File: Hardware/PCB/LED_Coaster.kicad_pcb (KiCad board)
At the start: 2 copper layers, 90 x 90 mm, 88 parts, among them J1 Li-po, J3 USB_C_Receptacle_USB2.0_16P, J4 UART, Q1 AO3401A, SW1 SW_SPDT, U1 ESP32-C3-WROOM-02-H4, U3 MCP73871-2CC, U4 TLV75533PDBVR

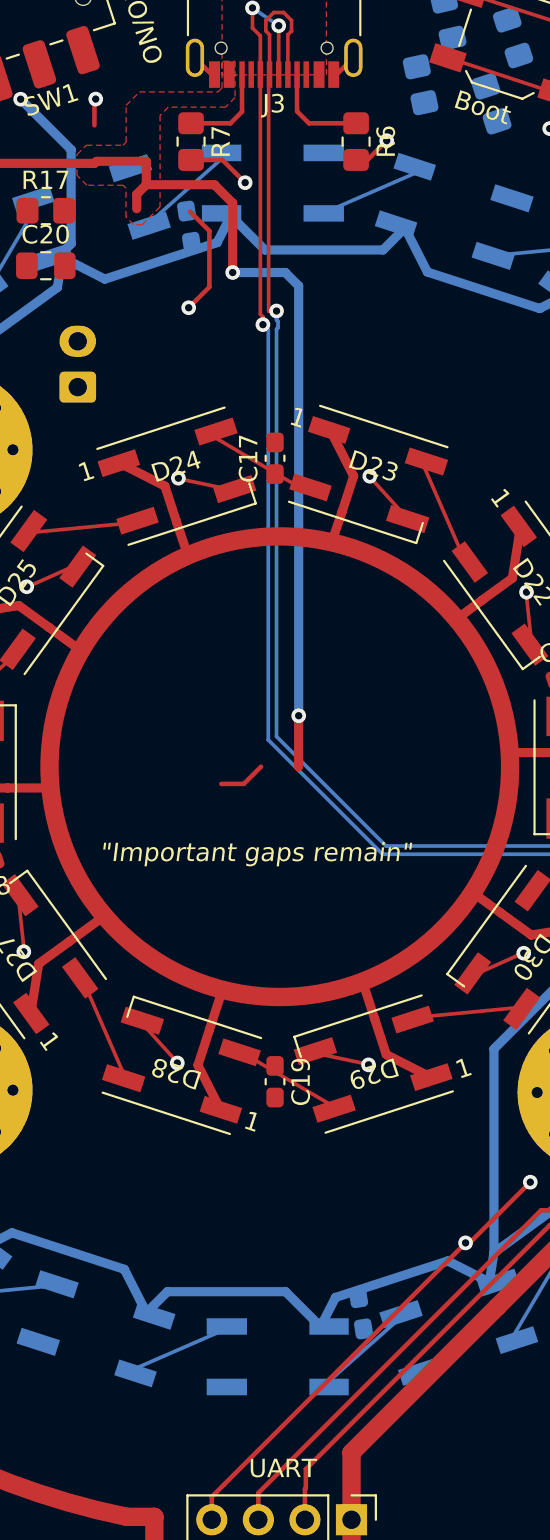
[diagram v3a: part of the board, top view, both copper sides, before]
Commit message: Move C10/C14 outward, and restructure Phase 5 as a numbered action list
C10 and C14 sit in the two tightest gaps on the outer ring, so at the exact
midpoint bearing they overlapped D7 and D17 by 0.07 mm. They were nudged 1°
sideways, which left them visibly off-centre in the slot. Moving them outward
to r = 35 instead puts them back on the midpoint bearing with the round
rotations the other six use, and widens their clearance to +1.40/+0.81 mm - the
roomiest on the ring. Outward also keeps every capacitor at or beyond the LED
radius, so nothing encroaches on the battery pocket in the middle of the back.

Phase 5 was hard to act on: reference material and steps were interleaved. It
is now one background block followed by nine numbered actions.

Action 2 is new. Deleting the three dead zones also removed the only GND zone
on F.Cu - it was a 3 x 4 mm scrap sitting on the old regulator. The back keeps
its board-wide pour but the front now has none, which is why 47 ground pads
read as isolated: every front LED D21-D30, all four buttons, the four front
decoupling caps and the whole new power section. A board-wide F.Cu GND zone
connects them in one step.

Connectivity re-measured with all 34 parts placed, so the scope table is
current: +LED_PWR needs ~40 connections (46 pads in 41 groups), +SYS 8,
+BATT 5, /BAT_SENSE 3, +3V3 2, plus the 28 LED data hops.

Co-Authored-By: Claude Opus 5 <noreply@anthropic.com>
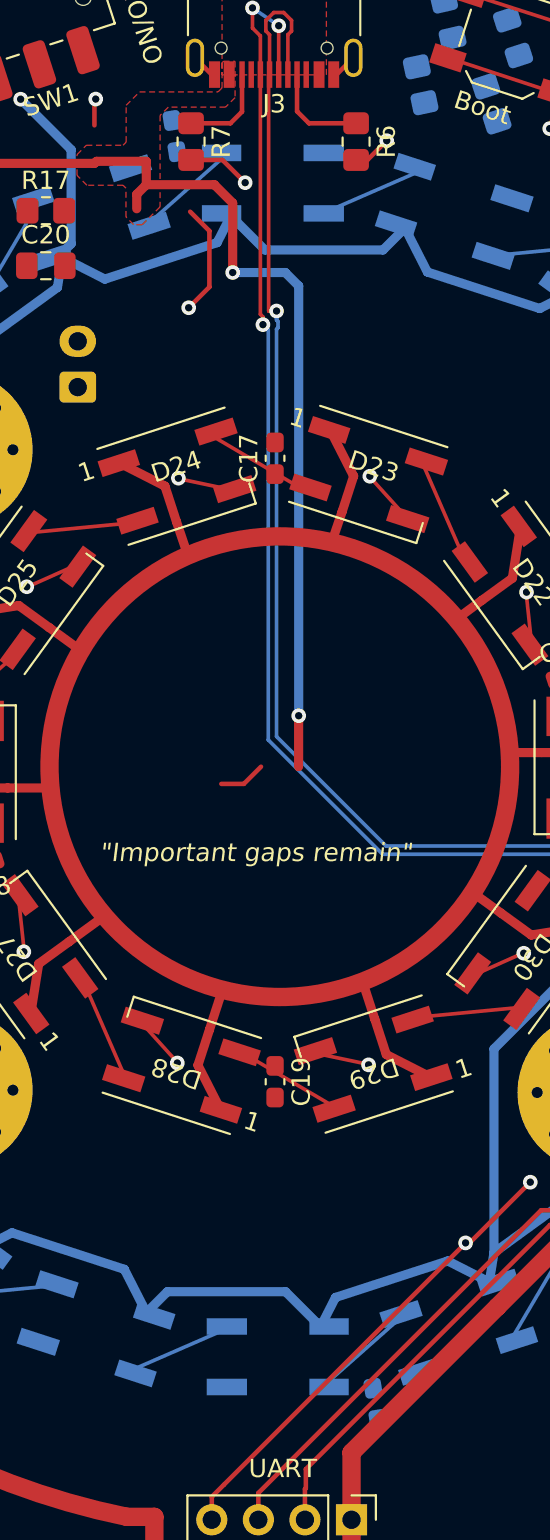
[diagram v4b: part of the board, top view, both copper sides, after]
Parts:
- moved C10 5.00 mm to (144.5, 45.4)
- moved C14 5.00 mm to (155.5, 114.6)
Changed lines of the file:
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@@
 	(footprint "Capacitor_SMD:C_0603_1608Metric_Pad1.08x0.95mm_HandSolder"
 		(layer "B.Cu")
-		(at 145.31 50.37 99)
+		(at 144.52 45.43 99)
 		(descr "Capacitor SMD 0603 (1608 Metric), square (rectangular) end terminal, IPC-7351 nominal with elongated pad for handsoldering. (Body size source: IPC-SM-782 page 76, https://www.pcb-3d.com/wordpress/wp-content/uploads/ipc-sm-782a_amendment_1_and_2.pdf)")
 		(tags "capacitor handsolder")
@@
 	(footprint "Capacitor_SMD:C_0603_1608Metric_Pad1.08x0.95mm_HandSolder"
 		(layer "B.Cu")
-		(at 154.69 109.63 -81)
+		(at 155.48 114.57 -81)
 		(descr "Capacitor SMD 0603 (1608 Metric), square (rectangular) end terminal, IPC-7351 nominal with elongated pad for handsoldering. (Body size source: IPC-SM-782 page 76, https://www.pcb-3d.com/wordpress/wp-content/uploads/ipc-sm-782a_amendment_1_and_2.pdf)")
 		(tags "capacitor handsolder")

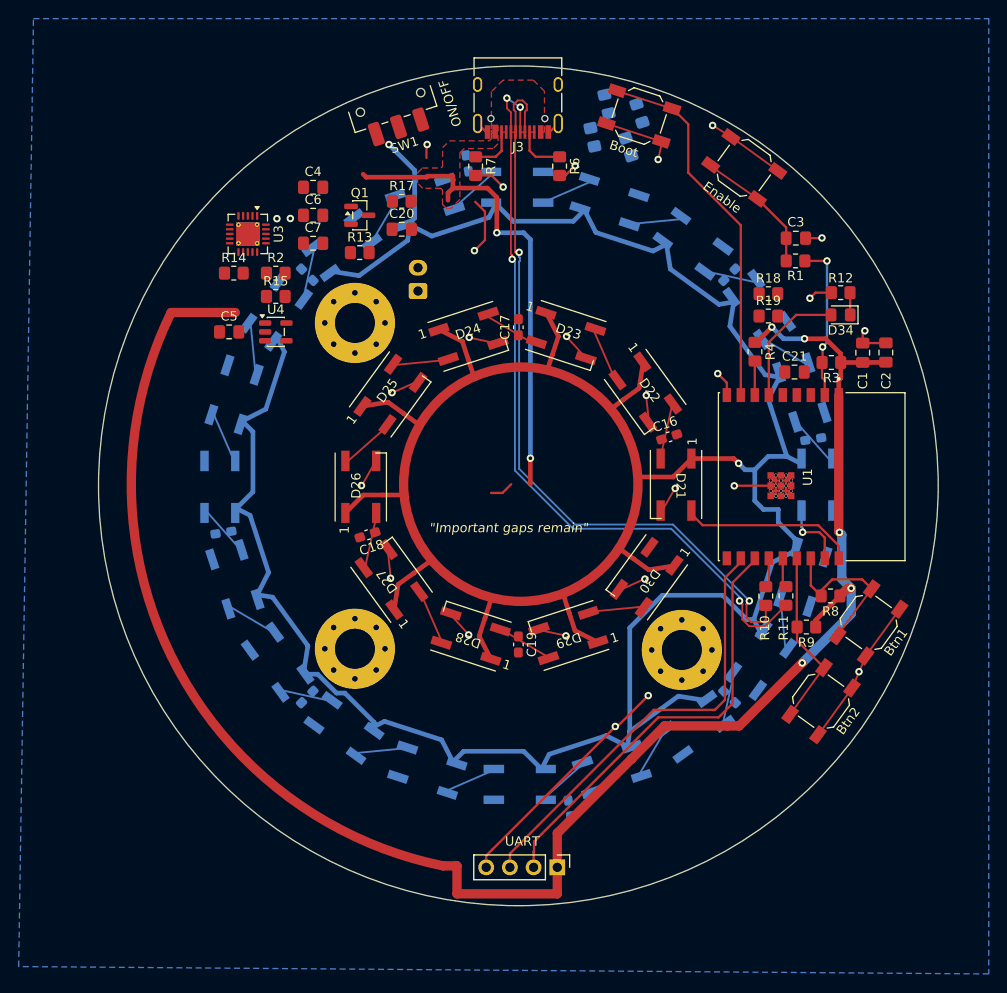
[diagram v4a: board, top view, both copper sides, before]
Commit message: Add pcb_check.py, a standalone board analysis tool, and document it
Every board question in this project so far has been answered by writing a
throwaway parser, and several of those parsers were wrong in ways that produced
confident bad advice. This commits one tool instead, and records the traps.

Hardware/PCB/tools/pcb_check.py reads LED_Coaster.kicad_pcb directly - stdlib
only, no KiCad install. Subcommands: nets, net <NAME>, shorts, rings, zones,
widths, placement, all. KiCad DRC stays the authority on manufacturability;
this answers what DRC does not, namely whether a net is genuinely one island
and which pad is stranded.

Six parsing traps are encoded in the header comment, each of which caused a
wrong answer at least once:

- Back-side pads are NOT X-mirrored. Mirroring swaps pad 3 for pad 4, invents
  shorts, and made a uniform LED ring look like it fanned through five
  orientations. Caught only when the PCB editor was read directly.
- A track end inside a via's pad radius is connected, not merely near it.
- Zone fills carry a per-polygon layer tag; one zone can span both sides.
- Same-net zones whose fills touch are one island, and priority decides
  overlaps, so a higher-priority zone can orphan a lower one.
- Pads sharing a number on one footprint are internally connected.
- Fine-pitch rectangular pads must not be approximated by their circumradius.

Also commits the routing done in Phase 5 actions 1-7.

Co-Authored-By: Claude Opus 5 <noreply@anthropic.com>
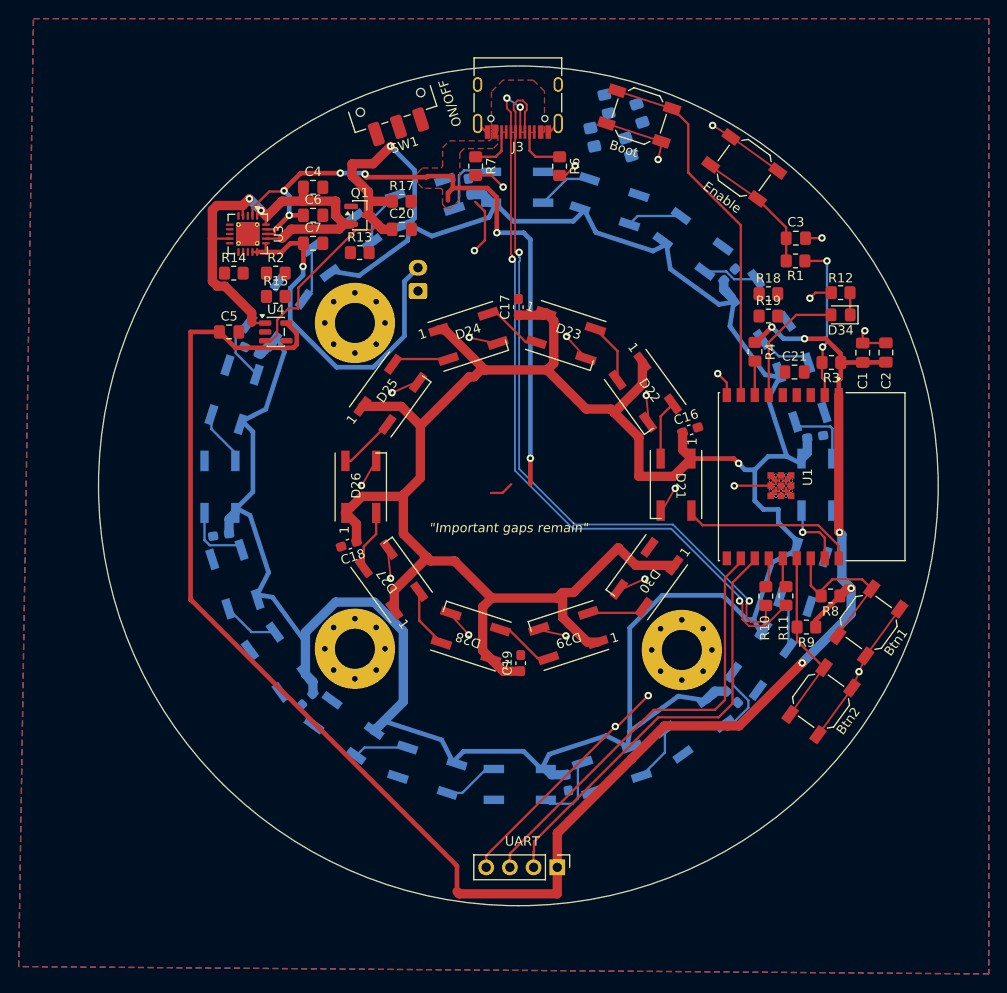
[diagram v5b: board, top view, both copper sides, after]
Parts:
- moved C11 10.1 mm to (121.4, 65.5), turned to 155 degrees
- moved C14 2.76 mm to (155.2, 111.8)
- moved C10 2.51 mm to (144.8, 47.9)
- moved C16 2.37 mm to (168.4, 74.0)
- moved C18 2.24 mm to (131.8, 86.2)
- moved C17 2.16 mm to (150.0, 60.8)
- moved C19 2.02 mm to (150.2, 99.0), turned to 90 degrees
- moved C12 0.35 mm to (118.1, 85.3)
- moved C8 0.33 mm to (181.8, 74.7)
- moved C15 0.25 mm to (172.9, 102.6)
- moved C13 0.25 mm to (127.4, 102.9)
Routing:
- net +LED_PWR: track 290.8 -> 473.6 mm
- net +3V3: track 95.3 -> 196.0 mm
- net +SYS: track 0.00 -> 49.7 mm, vias 0 -> 2
- net +BATT: track 0.00 -> 39.4 mm, vias 0 -> 1
- net +5V: track 51.6 -> 75.2 mm, vias 2 -> 6
- net Net-(D16-DOUT): track 0.00 -> 7.91 mm
- net Net-(D18-DOUT): track 0.00 -> 7.69 mm
- net Net-(D6-DOUT): track 0.00 -> 7.56 mm
- net Net-(D1-DOUT): track 0.00 -> 7.54 mm
- net Net-(D11-DOUT): track 0.00 -> 7.33 mm
- net Net-(D10-DIN): track 0.00 -> 7.03 mm
- net Net-(D22-DOUT): track 0.00 -> 6.46 mm
- net Net-(D27-DOUT): track 0.00 -> 6.45 mm
- net Net-(D28-DOUT): track 0.00 -> 6.43 mm
- net Net-(D26-DOUT): track 0.00 -> 6.42 mm
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- added copper zone on F.Cu, net GND

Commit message: Close the last outer-ring data hop, D13 to D14
Five B.Cu segments detouring around C13. That completes phase 5
action 5: the outer chain is 19 of 19 hops, and with the inner ring
already done both data chains are continuous end to end.

Co-Authored-By: Claude Opus 5 <noreply@anthropic.com>
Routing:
- net Net-(D13-DOUT): track 0.00 -> 7.57 mm
- net GND: track 72.2 -> 74.3 mm
- net +SYS: track 49.7 -> 50.4 mm
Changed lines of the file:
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@@
 	)
 	(segment
+		(start 121 50.106808)
+		(end 121.051808 50.055)
+		(width 0.25)
+		(layer "F.Cu")
+		(net "GND")
+	)
+	(segment
 		(start 182.52 53.45)
 		(end 182.54 53.43)
@@
 	)
 	(segment
+		(start 121 51.0625)
+		(end 121 50.106808)
+		(width 0.25)
+		(layer "F.Cu")
+		(net "GND")
+	)
+	(segment
 		(start 179.24 80.529999)
 		(end 177.040004 80.529999)
@@
 	)
 	(segment
+		(start 119.0625 54)
+		(end 119.0625 54.6225)
+		(width 0.25)
+		(layer "F.Cu")
+		(net "GND")
+	)
+	(segment
 		(start 177.589999 79.98)
 		(end 177.59 79.980001)
@@
 	)
 	(segment
+		(start 119.67 54.98)
+		(end 119.7125 54.9375)
+		(width 0.25)
+		(layer "F.Cu")
+		(net "GND")
+	)
+	(segment
 		(start 178.69 81.079996)
 		(end 178.690002 81.079998)
@@
 	)
 	(segment
+		(start 119.0625 54.6225)
+		(end 119.17 54.73)
+		(width 0.25)
+		(layer "F.Cu")
+		(net "GND")
+	)
+	(segment
 		(start 146.55 120.89)
 		(end 146.55 119.64)
@@
 	)
 	(segment
+		(start 120 54.9375)
+		(end 119.7125 54.9375)
+		(width 0.25)
+		(layer "F.Cu")
+		(net "GND")
+	)
+	(segment
 		(start 155.04 46.73)
 		(end 156.09 45.68)
@@
 	)
 	(segment
-		(start 117.2 53.48)
-		(end 117.2 50.45)
-		(width 1)
-		(layer "F.Cu")
-		(net "+SYS")
-	)
-	(segment
 		(start 122.9375 53.5)
 		(end 124.65 53.5)
@@
 	)
 	(segment
+		(start 120.42 49.23)
+		(end 121.17 49.23)
+		(width 1)
+		(layer "F.Cu")
+		(net "+SYS")
+	)
+	(segment
+		(start 120.45 51.0125)
+		(end 120.45 49.26)
+		(width 0.25)
+		(layer "F.Cu")
+		(net "+SYS")
+	)
+	(segment
 		(start 125.67 52.48)
 		(end 124.67 53.48)
@@
 	)
 	(segment
+		(start 117.2 53.48)
+		(end 117.2 50.45)
+		(width 1)
+		(layer "F.Cu")
+		(net "+SYS")
+	)
+	(segment
 		(start 124.67 49.48)
 		(end 123.040035 51.109965)
@@
 	)
 	(segment
+		(start 120.45 49.26)
+		(end 120.42 49.23)
+		(width 0.25)
+		(layer "F.Cu")
+		(net "+SYS")
+	)
+	(segment
 		(start 117.74957 58.6)
 		(end 117.2 58.05043)
@@
 	)
 	(segment
-		(start 120.5 51.0625)
-		(end 120.45 51.0125)
-		(width 0.25)
+		(start 117.2 50.45)
+		(end 118.42 49.23)
+		(width 1)
 		(layer "F.Cu")
 		(net "+SYS")
@@
 	)
 	(segment
+		(start 118.42 49.23)
+		(end 120.42 49.23)
+		(width 1)
+		(layer "F.Cu")
+		(net "+SYS")
+	)
+	(segment
 		(start 117.22 53.5)
 		(end 117.2 53.48)
@@
 	)
 	(segment
-		(start 120.45 51.0125)
-		(end 120.45 49.95)
-		(width 0.25)
-		(layer "F.Cu")
-		(net "+SYS")
-	)
-	(segment
-		(start 121.17 49.23)
-		(end 120.45 49.95)
-		(width 1)
-		(layer "F.Cu")
-		(net "+SYS")
-	)
-	(segment
 		(start 130.795001 52.48)
 		(end 125.67 52.48)
@@
 	)
 	(segment
-		(start 120.45 49.95)
-		(end 117.7 49.95)
-		(width 1)
-		(layer "F.Cu")
-		(net "+SYS")
-	)
-	(segment
 		(start 121.49 62.55)
 		(end 121.42 62.48)
@@
 	)
 	(segment
-		(start 117.2 50.45)
-		(end 117.7 49.95)
-		(width 1)
+		(start 122.8625 62.55)
+		(end 121.49 62.55)
+		(width 0.25)
 		(layer "F.Cu")
 		(net "+SYS")
 	)
 	(segment
-		(start 122.8625 62.55)
-		(end 121.49 62.55)
+		(start 120.5 51.0625)
+		(end 120.45 51.0125)
 		(width 0.25)
 		(layer "F.Cu")
@@
 	)
 	(segment
+		(start 127.17 104.48)
+		(end 128.661953 102.988047)
+		(width 0.25)
+		(layer "B.Cu")
+		(net "Net-(D13-DOUT)")
+	)
+	(segment
+		(start 126.09496 104.48)
+		(end 127.17 104.48)
+		(width 0.25)
+		(layer "B.Cu")
+		(net "Net-(D13-DOUT)")
+	)
+	(segment
+		(start 128.661953 102.988047)
+		(end 130.033538 102.988047)
+		(width 0.25)
+		(layer "B.Cu")
+		(net "Net-(D13-DOUT)")
+	)
+	(segment
+		(start 124.506324 102.125777)
+		(end 124.506324 102.891364)
+		(width 0.25)
+		(layer "B.Cu")
+		(net "Net-(D13-DOUT)")
+	)
+	(segment
+		(start 124.506324 102.891364)
+		(end 126.09496 104.48)
+		(width 0.25)
+		(layer "B.Cu")
+		(net "Net-(D13-DOUT)")
+	)
+	(segment
